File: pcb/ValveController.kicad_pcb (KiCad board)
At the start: 4 copper layers, 99 x 72 mm, 54 parts, among them J10 1770966, J11 1770966, J12 1770966, J13 USB4115-03-C, J2 1990986, J3 1990986, J8 1770966, J9 1770966, Q3 MOC3063S-TA1, Q4 MOC3063S-TA1, SW1 TL9320AF400QG, U1 IRM-03-5, U2 TLV75733P, U5 ESP32-C6-WROOM-1-N4

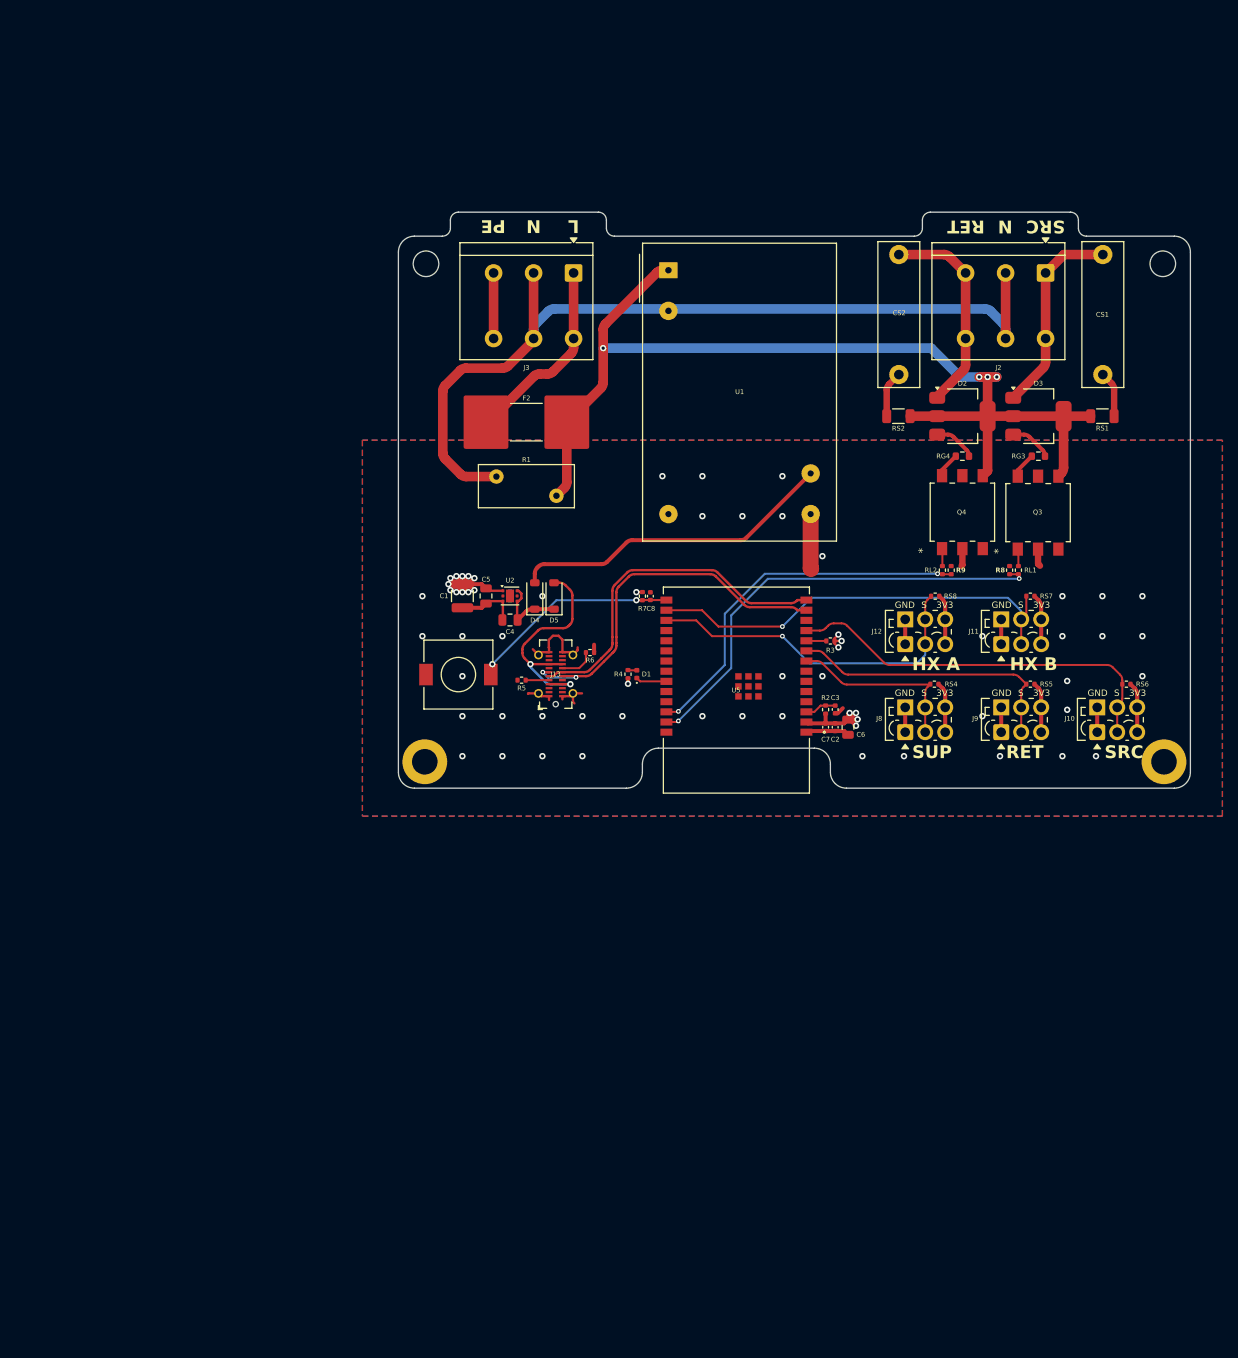
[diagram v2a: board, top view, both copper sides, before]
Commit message: feat(pcb): strip status LED, USB4145 connector, reorganise schematic
The 8x8 matrix display (DS1 + U7) supersedes the D1 status LED, so D1 goes
along with R4, its GPIO15 strap pull-up — GPIO15 is Ignored with the default
eFuses, leaving it and GPIO16 as the only clean non-strapping spares.

J13 swaps from GCT USB4115 to USB4145-03-0170-C: easier to hand-solder, no
shield tabs in front of the pins. The SnapMagic-derived footprint and STEP
are gitignored — their licence permits building boards, not redistributing
model files — so regenerate with tools/import_usb4145.py. The two hand-drawn
peg keepouts are dropped; they were cut for the USB4115 body and fouled the
new 1.15 mm contact row. The abandoned UJ20 library goes with them.

Schematic reorganised into labelled functional groups: 59 footprint,
datasheet and description fields hidden (they were printing full DigiKey
URLs and library paths across the sheet), 32 field-name prefixes normalised,
30 global labels turned to read away from their own parts instead of across
them, and all 103 clusters regrouped into three bands under 10 outlines.

Netlist is byte-identical and ERC unchanged at 130 violations, category for
category, across the whole reorganisation.
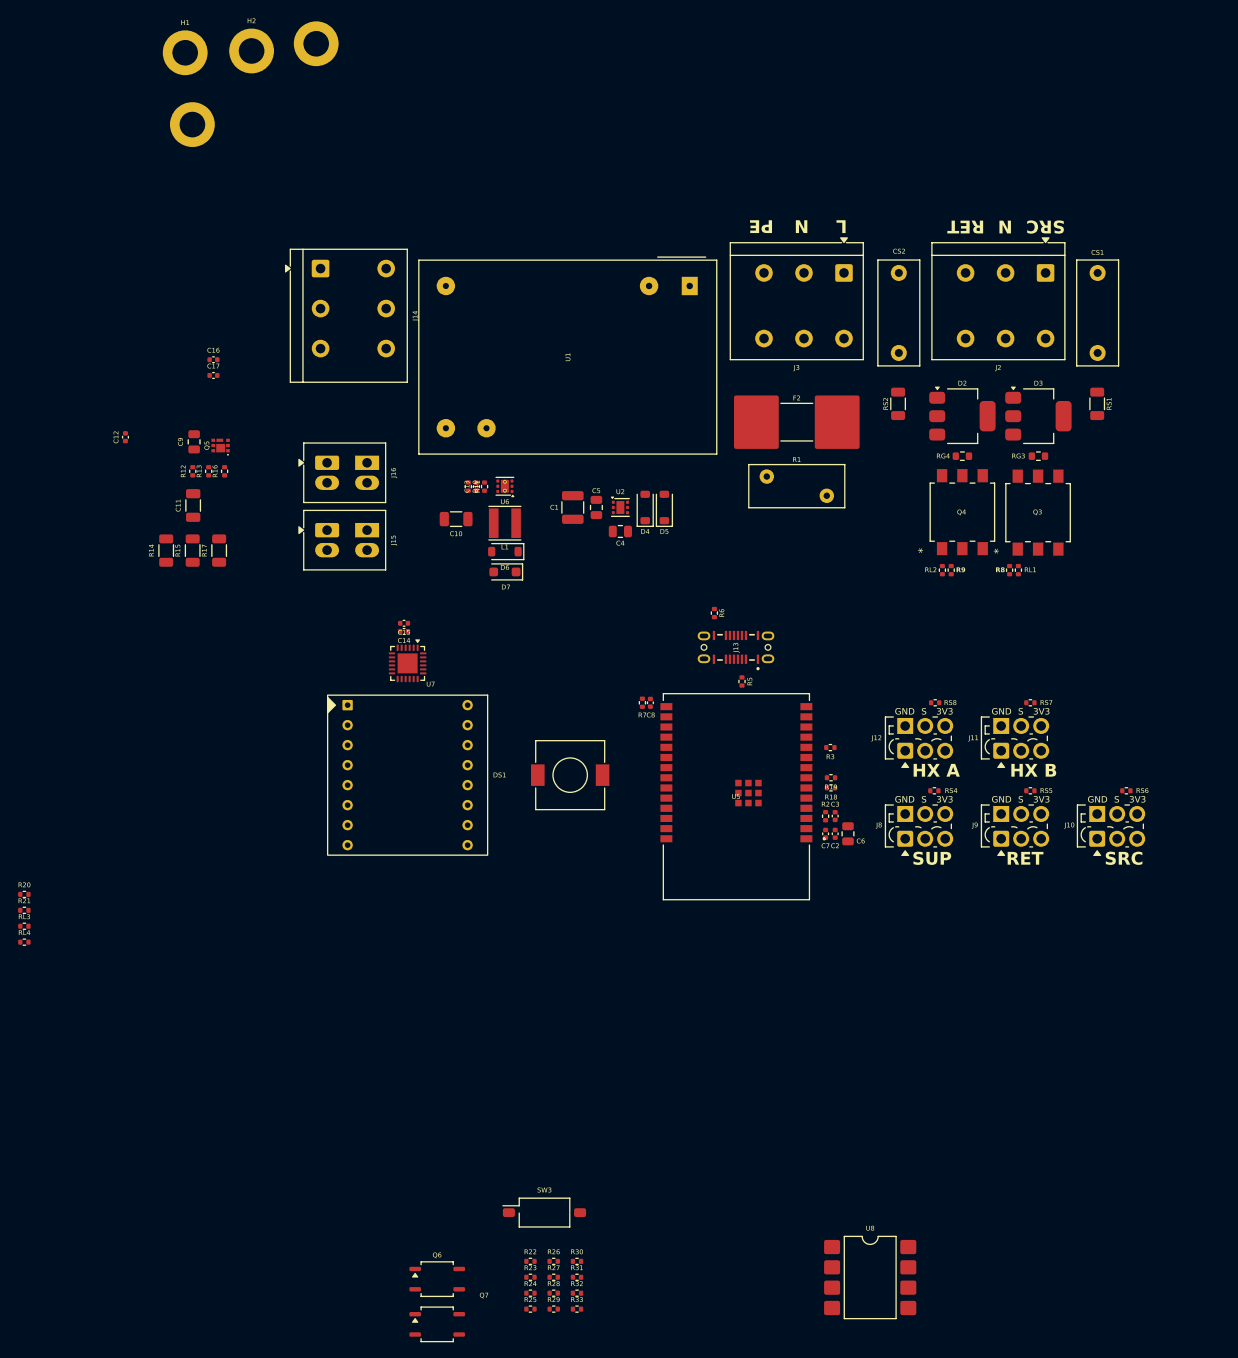
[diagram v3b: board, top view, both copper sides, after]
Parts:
- removed D1: LED (active-low), LED_SMD:LED_0402_1005Metric
- removed R4: 1k, Resistor_SMD:R_0402_1005Metric
- added C10: 2.2uF, Capacitor_SMD:C_1206_3216Metric, F.Cu at (69.2, 75.4)
- added C11: 2.2uF, Capacitor_SMD:C_1206_3216Metric, F.Cu at (36.3, 73.7)
- added C12: 10nF, Capacitor_SMD:C_0402_1005Metric, F.Cu at (27.9, 65.1)
- added C13: 82pF, Capacitor_SMD:C_0402_1005Metric, F.Cu at (71.8, 71.3)
- added C14: 100nF, Capacitor_SMD:C_0402_1005Metric, F.Cu at (62.7, 89.4)
- added C15: 1uF, Capacitor_SMD:C_0402_1005Metric, F.Cu at (62.7, 88.4)
- added C16: 100nF, Capacitor_SMD:C_0402_1005Metric, F.Cu at (38.9, 55.4)
- added C17: 100nF, Capacitor_SMD:C_0402_1005Metric, F.Cu at (38.9, 57.4)
- added C9: 4.7uF, Capacitor_SMD:C_0805_2012Metric, F.Cu at (36.5, 65.7)
- added D6: B5819W, Diode_SMD:D_SOD-123, F.Cu at (75.3, 79.4)
- added D7: BZT52B27, Diode_SMD:D_SOD-123F, F.Cu at (75.3, 82.0)
- added DS1: KWM-20881AGB, Kleist2:LED_Matrix_8x8_20mm, F.Cu at (63.2, 107.4)
- added J14: 1990986, Kleist2:TerminalBlock_Phoenix_SPT-2,5-3-H-5.0_1x03_P5.00mm_Horizontal, F.Cu at (52.3, 44.0)
- added J15: 1770885, TerminalBlock_Phoenix:TerminalBlock_Phoenix_PTSM-0,5-2-2.5-H-THR_1x02_P2.50mm_Horizontal, F.Cu at (53.1, 76.8)
- added J16: 1770885, TerminalBlock_Phoenix:TerminalBlock_Phoenix_PTSM-0,5-2-2.5-H-THR_1x02_P2.50mm_Horizontal, F.Cu at (53.1, 68.3)
- added L1: 10uH, Inductor_SMD:L_Taiyo-Yuden_NR-40xx, F.Cu at (75.3, 75.9)
- added Q5: CSD17313Q2, Kleist2:CSD17313Q2, F.Cu at (39.8, 66.2)
- added Q6: CPC1017N, Package_SO:SOP-4_3.8x4.1mm_P2.54mm, F.Cu at (66.8, 170.4)
- added Q7: CPC1017N, Package_SO:SOP-4_3.8x4.1mm_P2.54mm, F.Cu at (66.8, 176.0)
- added R10: 249k, Resistor_SMD:R_0402_1005Metric, F.Cu at (72.8, 71.3)
- added R11: 13.3k, Resistor_SMD:R_0402_1005Metric, F.Cu at (70.7, 71.3)
- added R12: 100, Resistor_SMD:R_0402_1005Metric, F.Cu at (36.3, 69.4)
- added R13: 10k, Resistor_SMD:R_0402_1005Metric, F.Cu at (38.3, 69.4)
- added R14: 2.2k, Resistor_SMD:R_1206_3216Metric, F.Cu at (33.0, 79.3)
- added R15: 100, Resistor_SMD:R_1206_3216Metric, F.Cu at (36.3, 79.3)
- added R16: 10k, Resistor_SMD:R_0402_1005Metric, F.Cu at (40.3, 69.4)
- added R17: 100, Resistor_SMD:R_1206_3216Metric, F.Cu at (39.6, 79.3)
- added R18: 4.7k, Resistor_SMD:R_0402_1005Metric, F.Cu at (116.1, 109.0)
- added R19: 4.7k, Resistor_SMD:R_0402_1005Metric, F.Cu at (116.1, 107.7)
- added R20: 10k, Resistor_SMD:R_0402_1005Metric, F.Cu at (15.2, 122.3)
- added R21: 10k, Resistor_SMD:R_0402_1005Metric, F.Cu at (15.2, 124.3)
- added R22: 10k, Resistor_SMD:R_0402_1005Metric, F.Cu at (78.5, 168.1)
- added R23: 4.7k, Resistor_SMD:R_0402_1005Metric, F.Cu at (78.5, 170.1)
- added R24: 10k, Resistor_SMD:R_0402_1005Metric, F.Cu at (78.5, 172.1)
- added R25: 4.7k, Resistor_SMD:R_0402_1005Metric, F.Cu at (78.5, 174.1)
- added R26: 10k, Resistor_SMD:R_0402_1005Metric, F.Cu at (81.4, 168.1)
- added R27: 10k, Resistor_SMD:R_0402_1005Metric, F.Cu at (81.4, 170.1)
- added R28: 10k, Resistor_SMD:R_0402_1005Metric, F.Cu at (81.4, 172.1)
- added R29: 10k, Resistor_SMD:R_0402_1005Metric, F.Cu at (81.4, 174.1)
- added R30: 1k, Resistor_SMD:R_0402_1005Metric, F.Cu at (84.3, 168.1)
- added R31: 1k, Resistor_SMD:R_0402_1005Metric, F.Cu at (84.3, 170.1)
- added R32: 100k, Resistor_SMD:R_0402_1005Metric, F.Cu at (84.3, 172.1)
- added R33: 100k, Resistor_SMD:R_0402_1005Metric, F.Cu at (84.3, 174.1)
- added RL3: 680, Resistor_SMD:R_0402_1005Metric, F.Cu at (15.2, 126.3)
- added RL4: 680, Resistor_SMD:R_0402_1005Metric, F.Cu at (15.2, 128.2)
- added SW3: A6S-1102-H, Button_Switch_SMD:SW_DIP_SPSTx01_Slide_Omron_A6S-110x_W8.9mm_P2.54mm, F.Cu at (80.3, 162.1)
- added U6: TPS61040, Package_SON:WSON-6-1EP_2x2mm_P0.65mm_EP1x1.6mm_ThermalVias, F.Cu at (75.3, 71.3)
- added U7: IS31FL3730, Package_DFN_QFN:QFN-24-1EP_4x4mm_P0.5mm_EP2.5x2.5mm, F.Cu at (63.2, 93.4)
- added U8: LTV-824S, Package_DIP:SMDIP-8_W9.53mm, F.Cu at (121.0, 170.2)
- CS1, CS2: value 22nF X2 -> 4.7nF X1/Y2; footprint Capacitor_THT:C_Rect_L18.0mm_W5.0mm_P15.00mm_FKS3_FKP3 -> Capacitor_THT:C_Rect_L13.0mm_W5.0mm_P10.00mm_FKS3_FKP3_MKS4
- H1, H2: footprint MountingHole:MountingHole_3.2mm_M3_DIN965 -> MountingHole:MountingHole_3.2mm_M3_DIN965_Pad
- J13: value USB4115-03-C -> USB4145-03-0170-C; footprint Connector_USB:USB_C_Receptacle_GCT_USB4115-03-C -> Kleist2:USB_C_Receptacle_GCT_USB4145-03-0170-C_Vertical_SMT
- moved H4 138.9 mm to (51.7, 15.9)
- moved H2 117.0 mm to (43.6, 16.9)
- moved H3 84.8 mm to (36.2, 26.1)
- moved H1 40.0 mm to (35.4, 17.1)
- moved F2 33.8 mm to (111.8, 63.2)
- moved J3 33.8 mm to (117.7, 44.6)
- moved R1 33.8 mm to (108.0, 70.0)
- moved R5 27.6 mm to (105.0, 95.7), turned to -90 degrees
- moved J13 22.8 mm to (104.2, 91.4), turned to 180 degrees
- moved SW1 18.8 mm to (83.5, 107.4)
- moved C1 17.7 mm to (83.8, 73.9)
- moved C4 17.7 mm to (89.8, 76.9)
- moved C5 17.7 mm to (86.8, 73.9)
- moved D4 17.7 mm to (92.8, 73.9)
- moved D5 17.7 mm to (95.2, 73.9)
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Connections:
- U5 pad 12: unconnected-(U5-IO11-Pad12) -> AUX1_DET
- U5 pad 18: unconnected-(U5-IO20-Pad18) -> PUMP_PWM
- U5 pad 19: unconnected-(U5-IO21-Pad19) -> PUMP_FB
- U5 pad 20: unconnected-(U5-IO22-Pad20) -> AUX1_EN
- U5 pad 21: unconnected-(U5-IO23-Pad21) -> AUX2_EN
- U5 pad 23: STAT_LED -> unconnected-(U5-IO15-Pad23)
- U5 pad 24: unconnected-(U5-RXD0-Pad24) -> AUX2_DET
- U5 pad 6: unconnected-(U5-IO6-Pad6) -> I2C_SDA
- U5 pad 7: unconnected-(U5-IO7-Pad7) -> I2C_SCL
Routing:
- net MAINS_L_F: track 130.3 -> 0.00 mm, vias 4 -> 0
- net MAINS_N: track 110.4 -> 0.00 mm
- net 3V3: track 66.9 -> 0.00 mm, vias 20 -> 0
- net GND: track 60.1 -> 0.00 mm, vias 43 -> 0
- net SSR_OPEN: track 57.1 -> 0.00 mm, vias 2 -> 0
- net TEMP_HX_A: track 54.7 -> 0.00 mm, vias 1 -> 0
- net TEMP_SOURCE: track 49.5 -> 0.00 mm
- net USB_D-: track 47.1 -> 0.00 mm, vias 2 -> 0
- net SSR_CLOSE: track 46.5 -> 0.00 mm, vias 2 -> 0
- net USB_D+: track 43.6 -> 0.00 mm
- net TEMP_HX_B: track 42.6 -> 0.00 mm, vias 1 -> 0
- net PSU_5V: track 40.8 -> 0.00 mm
- net TEMP_RETURN: track 35.3 -> 0.00 mm
- net VBUS: track 29.2 -> 0.00 mm, vias 2 -> 0
- net BOOT: track 26.7 -> 0.00 mm, vias 2 -> 0
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- removed copper zone on In2.Cu, net 3V3
- removed copper zone on B.Cu, net GND
- removed copper zone on F.Cu, net GND
- removed copper zone on In1.Cu, net GND
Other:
- board outline removed

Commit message: feat: update positioning
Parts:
- moved H3 150.3 mm to (152.0, 122.0)
- moved RL3 127.6 mm to (133.7, 78.7), turned to -90 degrees
- moved R20 125.3 mm to (132.7, 78.7), turned to -90 degrees
- moved RL4 125.2 mm to (133.5, 87.2), turned to -90 degrees
- moved R21 123.0 mm to (132.5, 87.2), turned to -90 degrees
- moved H1 117.2 mm to (152.0, 28.5)
- moved Q6 112.4 mm to (136.5, 82.2)
- moved Q7 110.1 mm to (136.5, 90.7)
- moved R23 110.0 mm to (139.6, 78.7), turned to -90 degrees
- moved R22 107.8 mm to (138.6, 78.7), turned to 90 degrees
- moved R27 107.3 mm to (137.6, 78.7), turned to -90 degrees
- moved H4 106.5 mm to (61.0, 122.0)
- moved R25 106.2 mm to (139.5, 87.2), turned to -90 degrees
- moved R26 105.1 mm to (136.6, 78.7), turned to 90 degrees
- moved R24 104.0 mm to (138.5, 87.2), turned to 90 degrees
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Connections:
- J15 pad 1: AUX1_IN -> AUX1_OUT
- J15 pad 2: AUX1_OUT -> AUX1_IN
- J16 pad 1: AUX2_IN -> AUX2_OUT
- J16 pad 2: AUX2_OUT -> AUX2_IN
- U8 pad 1: DET1_L -> DET2_L
- U8 pad 2: AUX1_OUT -> AUX2_OUT
- U8 pad 3: DET2_L -> DET1_L
- U8 pad 4: AUX2_OUT -> AUX1_OUT
- U8 pad 6: AUX2_DET -> AUX1_DET
- U8 pad 8: AUX1_DET -> AUX2_DET
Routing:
- net DISP_R3: track 0.00 -> 41.1 mm, vias 0 -> 2
- net AUX2_OUT: track 0.00 -> 30.9 mm
- net DISP_R4: track 0.00 -> 29.7 mm
- net GND: track 0.00 -> 29.4 mm, vias 0 -> 6
- net DISP_C1: track 0.00 -> 27.3 mm
- net 5V: track 0.00 -> 27.1 mm
- net DET1_L: track 0.00 -> 26.2 mm
- net DISP_R5: track 0.00 -> 25.9 mm
- net DISP_C8: track 0.00 -> 25.0 mm
- net AUX1_OUT: track 0.00 -> 24.0 mm
- net DISP_C2: track 0.00 -> 23.9 mm
- net DISP_R2: track 0.00 -> 23.8 mm, vias 0 -> 2
- net WET_24V: track 0.00 -> 21.7 mm, vias 0 -> 3
- net DISP_R6: track 0.00 -> 20.9 mm
- net DISP_R1: track 0.00 -> 19.8 mm, vias 0 -> 2
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- added copper zone on In2.Cu, net 3V3
- added copper zone on B.Cu, net GND
- added copper zone on F.Cu, net GND
- added copper zone on In1.Cu, net GND
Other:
- board text removed: "ISOLATION BARRIER - keep >=8mm, no copper crossing"
